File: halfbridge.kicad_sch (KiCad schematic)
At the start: 43 parts, among them Q5 Q_NIGBT_GCE, Q6 Q_NIGBT_GCE, U10 ADuM121N, U12 SO8 GATE DRVR, U13 SO8 GATE DRVR, U17 ACS730xLCTR-50AB, U6 SN6505BDBV, U9 ADuM121N

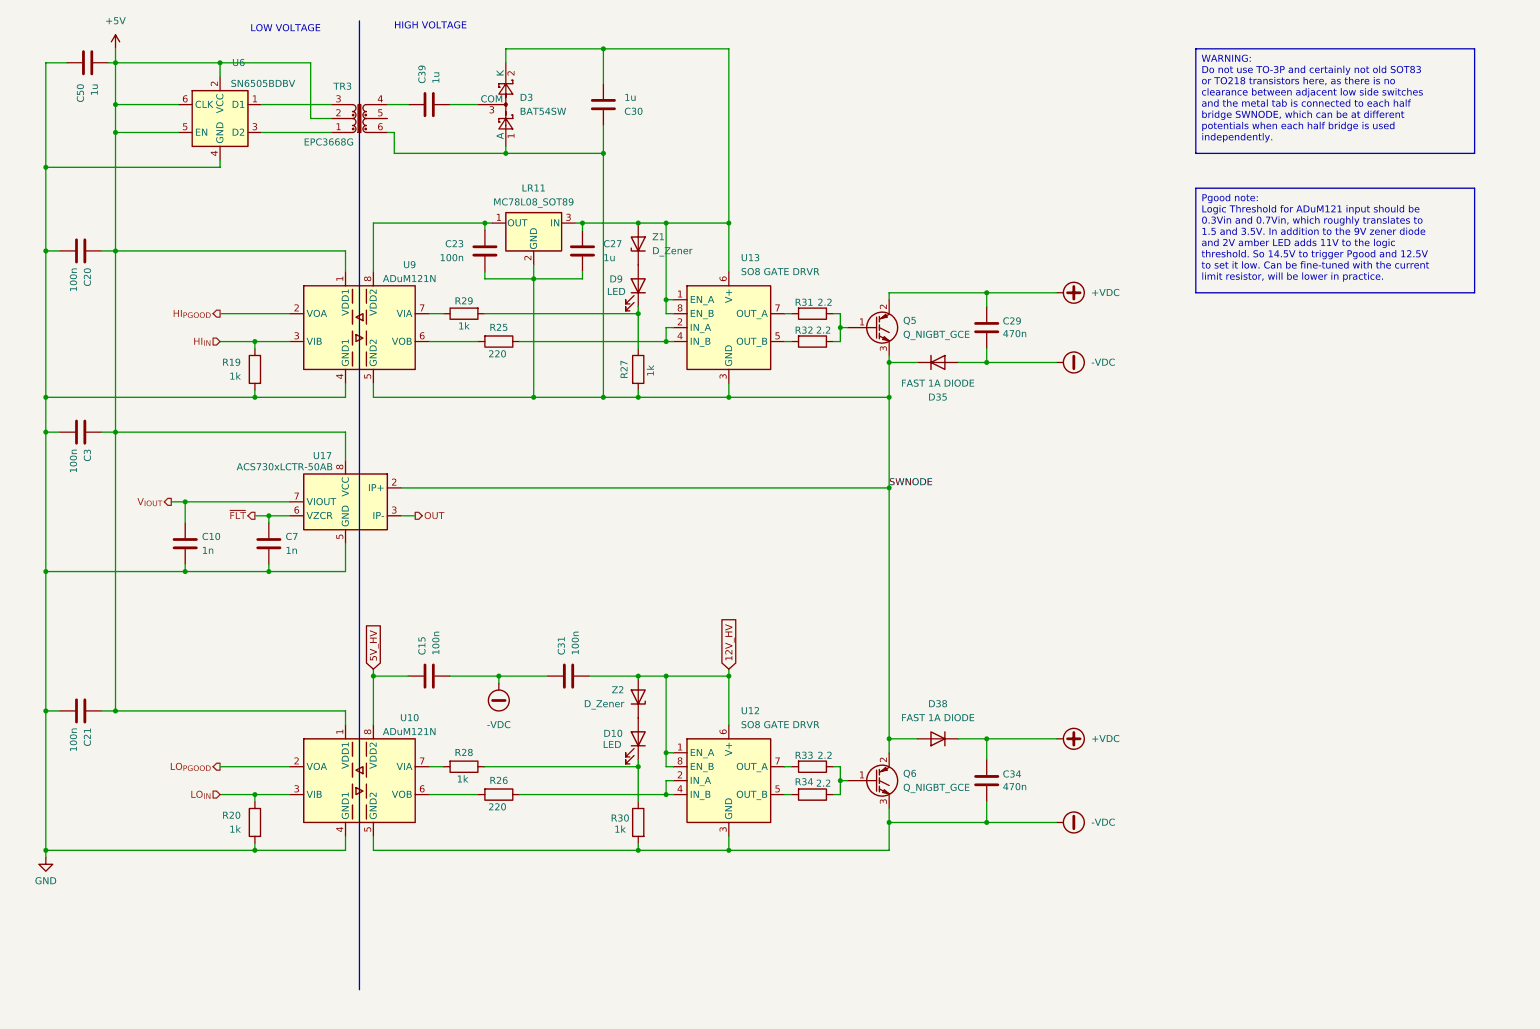
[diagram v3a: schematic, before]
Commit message: beginings of the implementation of the 10 open issues
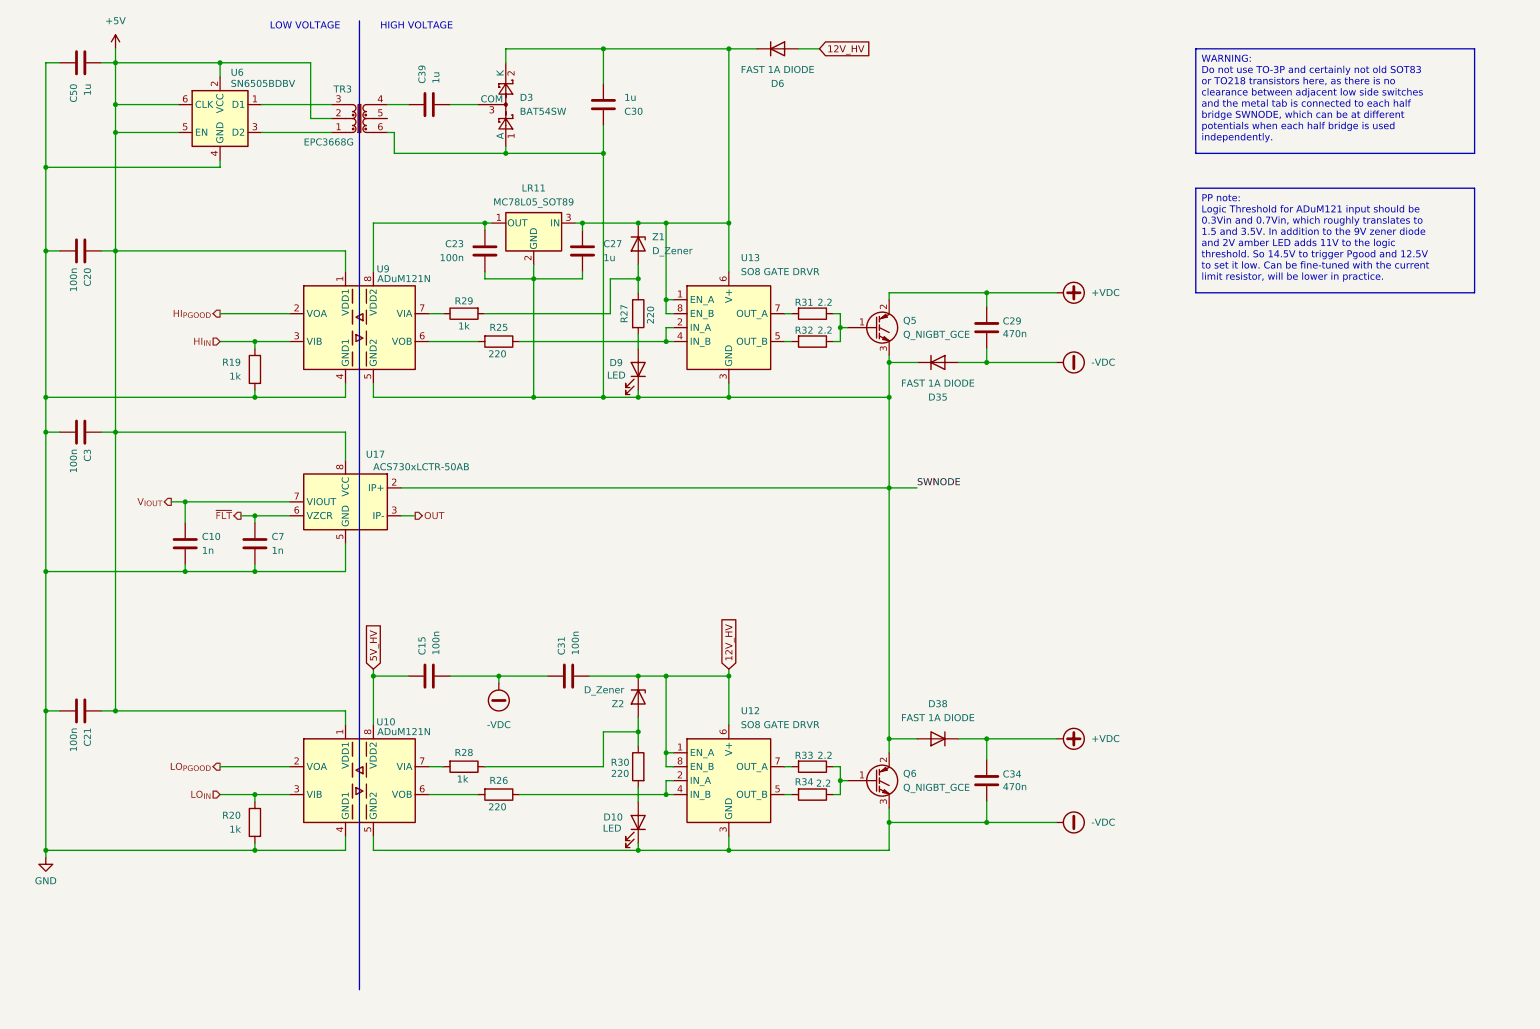
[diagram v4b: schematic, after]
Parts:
- added D6: FAST 1A DIODE, Diode_SMD:D_SOD-128, symbol Diode:1N4148WT
- LR11: value MC78L08_SOT89 -> MC78L05_SOT89
- R27, R30: value 1k -> 220
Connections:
- net -VDC: now also D10.1 (K); no longer R30.2
- net 12V_HV: now also Z2.1 (K), D6.2 (A); no longer Z2.2 (A)
- net SWNODE: now also D9.1 (K); no longer R27.2
- net at R28.1, R30.1: now also Z2.2 (A); no longer D10.1 (K)
- net at C27.1, C30.2, D3.2 (K)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: now also Z1.1 (K), D6.1 (K); no longer Z1.2 (A)
- net at R27.1, R29.2: now also Z1.2 (A); no longer D9.1 (K)
- net at D10.2 (A): now also R30.2; no longer Z2.1 (K)
- net at D9.2 (A): now also R27.2; no longer Z1.1 (K)
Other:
- moved on the sheet: C50, C7, D10, D9, R27, R30, Z1

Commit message: fixed many issues from previous itteration, added design rule checks to enforce minumum 2mm clearence between LV and HV side
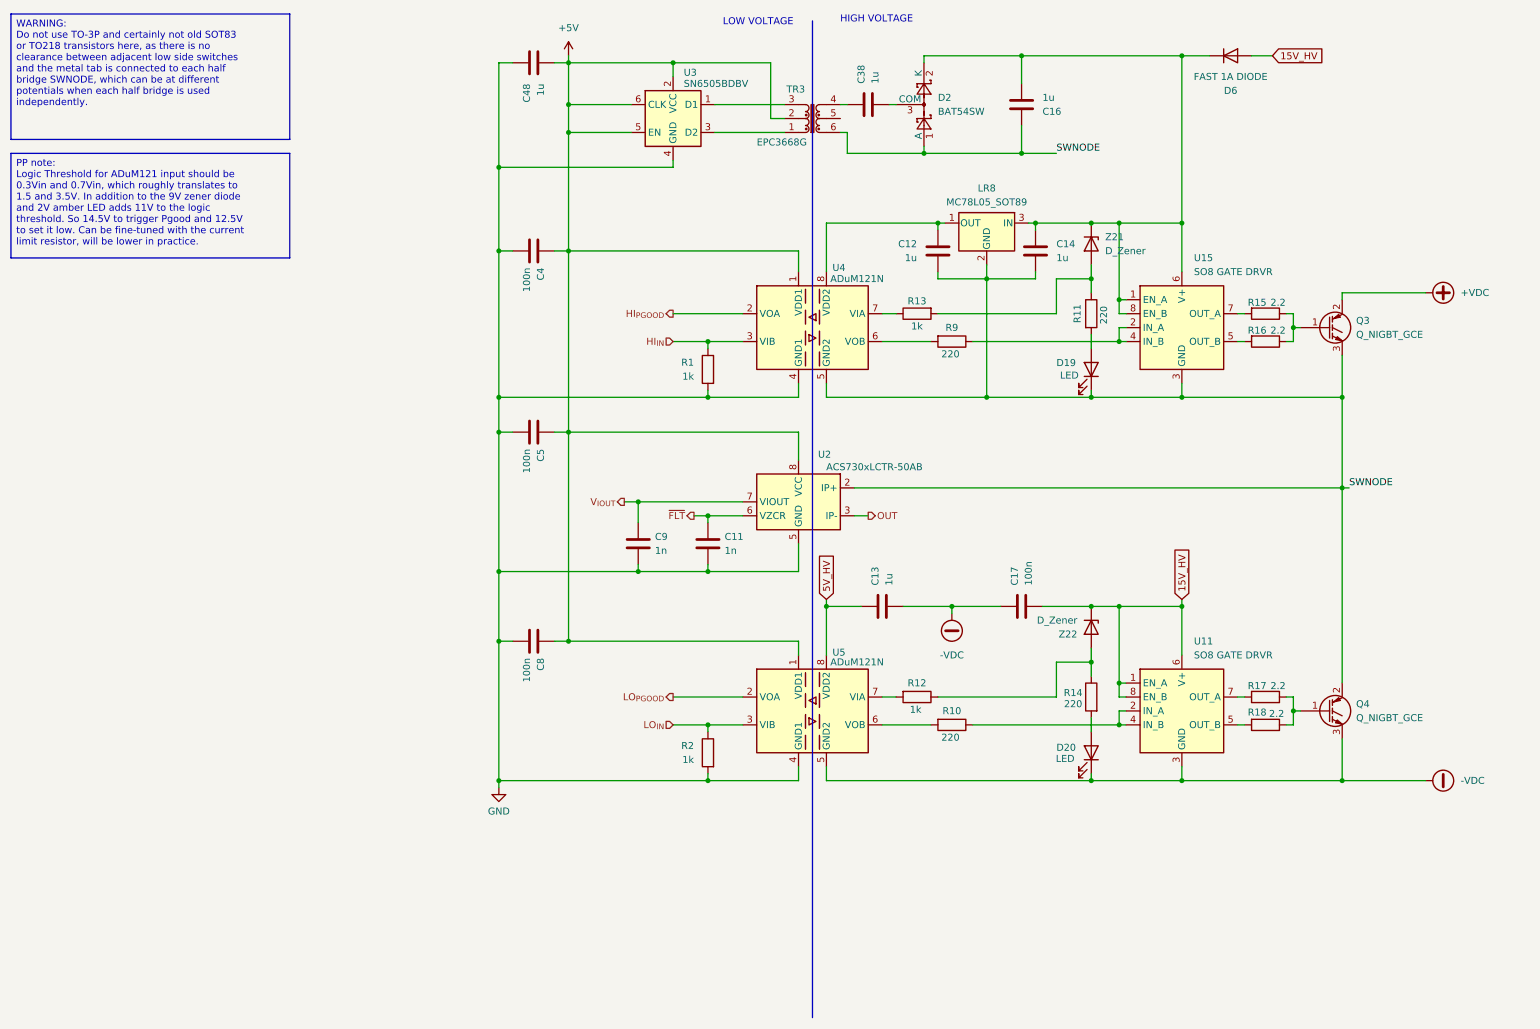
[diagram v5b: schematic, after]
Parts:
- removed C29, C34: 470n, Capacitor_SMD:C_1812_4532Metric, symbol Device:C
- removed D35, D38: FAST 1A DIODE, Diode_SMD:D_SOD-128, symbol Diode:1N4148WT
- C12: renamed from C23; value 100n -> 1u
- C13: renamed from C15; value 100n -> 1u
- D19: renamed from D9; footprint Capacitor_SMD:C_0805_2012Metric -> LED_SMD:LED_0805_2012Metric
- renumbered C7 to C11, C27 to C14, C30 to C16, C31 to C17, C39 to C38, C20 to C4, C50 to C48, C3 to C5, C21 to C8, C10 to C9, D3 to D2, D10 to D20, LR11 to LR8, Q5 to Q3, Q6 to Q4, R19 to R1, R26 to R10, R27 to R11, R28 to R12, R29 to R13, R30 to R14, R31 to R15, R32 to R16, R33 to R17, R34 to R18, R20 to R2, R25 to R9, U12 to U11, U13 to U15, U17 to U2, U6 to U3, U9 to U4, U10 to U5, Z1 to Z21, Z2 to Z22
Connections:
- net 12V_HV renamed 15V_HV
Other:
- moved on the sheet: C11, C12, C13, C14, C16, C17, C38, C4, C48, C5, C8, C9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
